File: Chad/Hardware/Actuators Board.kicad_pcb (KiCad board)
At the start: 4 copper layers, 50 x 50 mm, 130 parts, among them IC1 BD62120AEFJ-E2, J1 Conn_01x05_Male, J2 Solenoid(Sol), J3 USB_C_Receptacle_USB2.0, J4 Conn_01x03_Male, J5 Conn_01x06_Male, J6 Conn_01x02_Male, Q1 MMDT2222A, Q2 SI2366DS, U1 ESP32-PICO-D4, U2 TPS54233D, U3 CP2102-GMR-QFN28, U4 SN65HVD230, U5 LTC4411, U6 RT9025-25GSP, U7 LTC4411

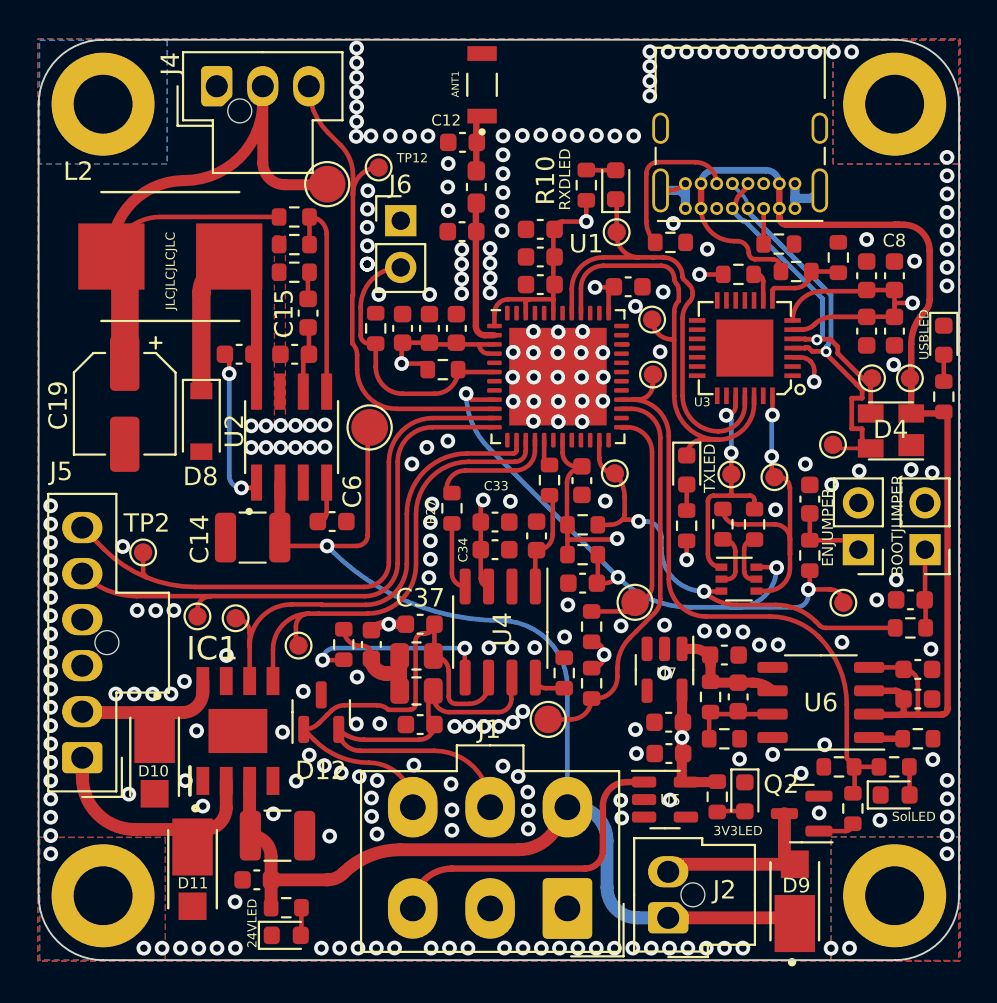
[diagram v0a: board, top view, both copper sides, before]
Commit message: Cut down on the number of vias, changed folder structure
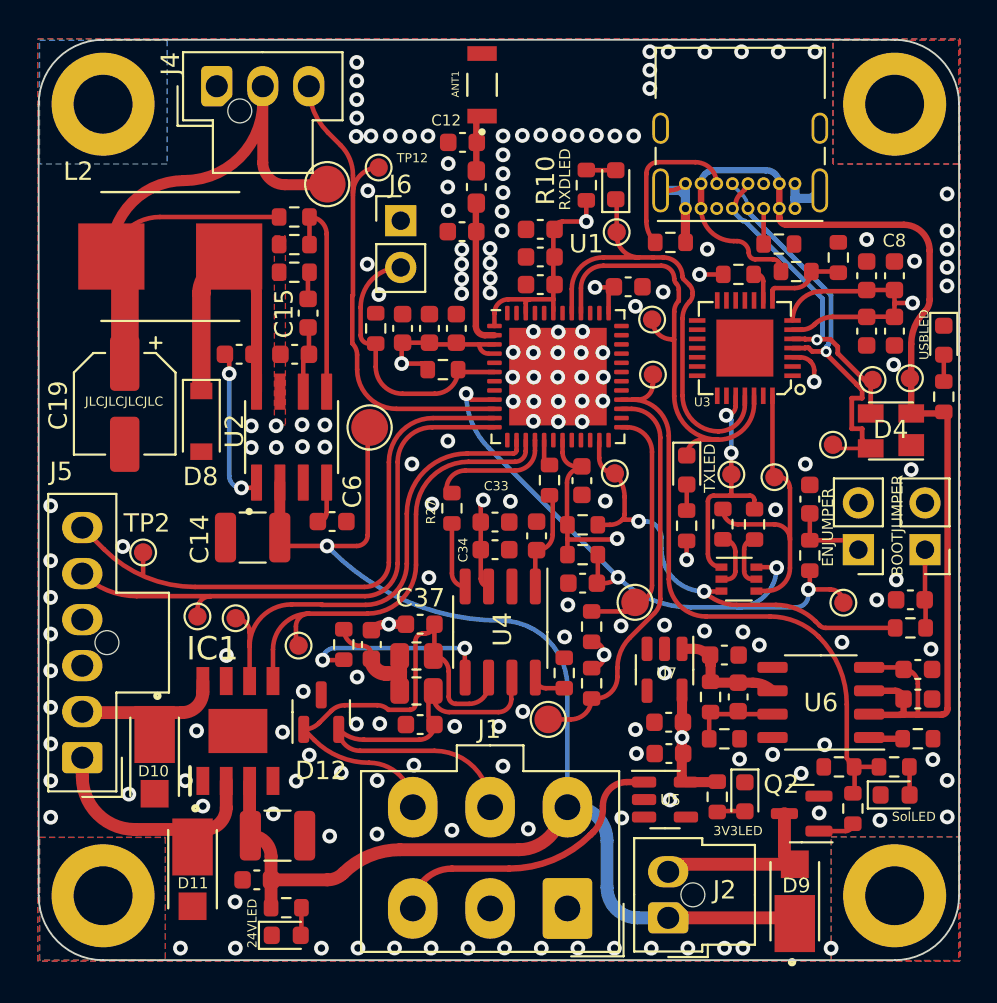
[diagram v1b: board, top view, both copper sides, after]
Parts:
- moved TP17 0.09 mm to (100.3, 48.5)
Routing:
- net /Motor+: track 14.7 -> 11.1 mm
- net +24V: track 79.9 -> 76.9 mm
- net +6V: track 38.6 -> 36.2 mm
- net /Motor-: track 10.1 -> 7.80 mm
- net VBUS: track 64.2 -> 62.2 mm
- net +3V3: track 64.6 -> 62.9 mm
- net /CAN_HIGH: track 25.1 -> 23.6 mm
- net /DTR: track 18.1 -> 16.6 mm, vias 2 -> 0
- net GND: track 11.6 -> 13.1 mm, vias 256 -> 171
- net Net-(J1-Pad3): track 17.4 -> 15.9 mm
- net /CAN_LOW: track 27.8 -> 26.7 mm
- net Net-(C1-Pad1): track 4.39 -> 3.59 mm
- net /USB -> UART/Data+: track 22.9 -> 22.3 mm
- net Net-(C35-Pad1): track 6.77 -> 6.14 mm
- net /SolEN: track 33.6 -> 33.0 mm
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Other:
- board text added: "C.H.A.D-v1"
- board text removed: "C.H.A.D - v1"

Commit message: Implemented design review feedback
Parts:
- removed TP22, TP25: TestPoint, TestPoint:TestPoint_Pad_D1.5mm
- added J7: Endstop Switch 1, TestPoint:TestPoint_Pad_D1.5mm, F.Cu at (87.4, 60.6)
- added J8: Endstop Switch 2, TestPoint:TestPoint_Pad_D1.5mm, F.Cu at (82.7, 66.9)
- 3V3LED1: renamed from 3V3LED; value PWR_LED -> 3V3LED
- C1, C2, C3: value 1uF -> 0.1uF
- C24: value 0.1uF -> 10uF
- L2: value ETQP5M -> 33uH
- moved TP17 0.14 mm to (100.4, 48.4)
- renumbered 24VLED to 24VLED1, BOOTJUMPER to BOOTJUMPER1, ENJUMPER to ENJUMPER1, RXDLED to RXLED1, SolLED to SolLED1, TXLED to TXLED1, USBLED to USBLED1
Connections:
- R19 pad 2: GND -> +3V3
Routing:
- net GND: track 13.1 -> 19.2 mm, vias 171 -> 170
- net +3V3: track 62.9 -> 64.1 mm, vias 10 -> 11
- net /USB -> UART/Data-: track 19.8 -> 20.4 mm
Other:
- board text added: "24VLED"
- board text added: "24V_TP"
- board text added: "3V3LED"
- board text added: "6V_TP"
- board text added: "BOOTJUMPER"
- board text added: "DCMotor_Conn"
- board text added: "DTR_TP"
- board text added: "DirPin1_TP"
- board text added: "DirPin2_TP"
- board text added: "ENJUMPER"
- board text added: "ES1Pad"
- board text added: "ES2Pad"
- board text added: "HallS1_TP"
- board text added: "HallS2_TP"
- board text added: "RBUS"
- board text added: "RTS_TP"
- board text added: "RXLED"
- board text added: "SSR_Conn"
- board text added: "ServoPWM_TP"
- board text added: "Servo_Conn"
- board text added: "SolLED"
- board text added: "Sol_Conn"
- board text added: "TXLED"
- board text added: "USBLED"

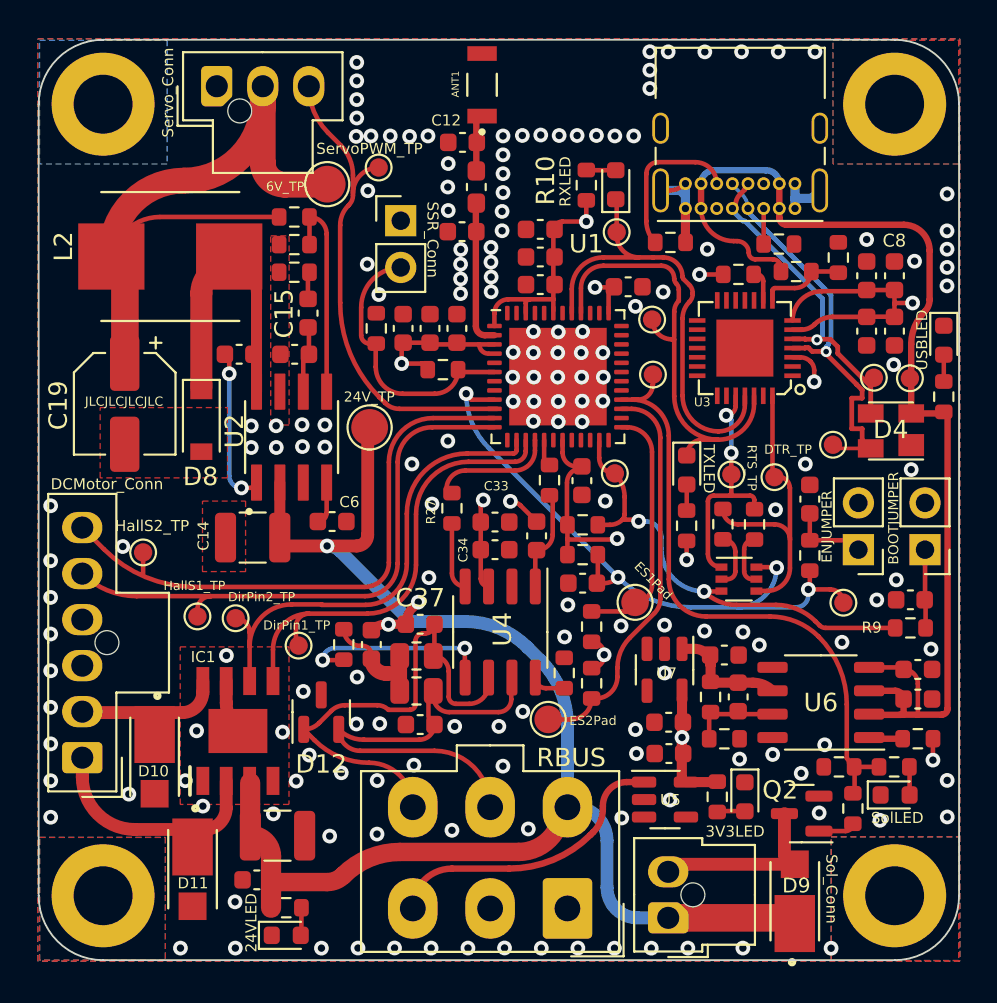
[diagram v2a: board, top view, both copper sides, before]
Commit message: Reduced thermal relief for the higher current connectors
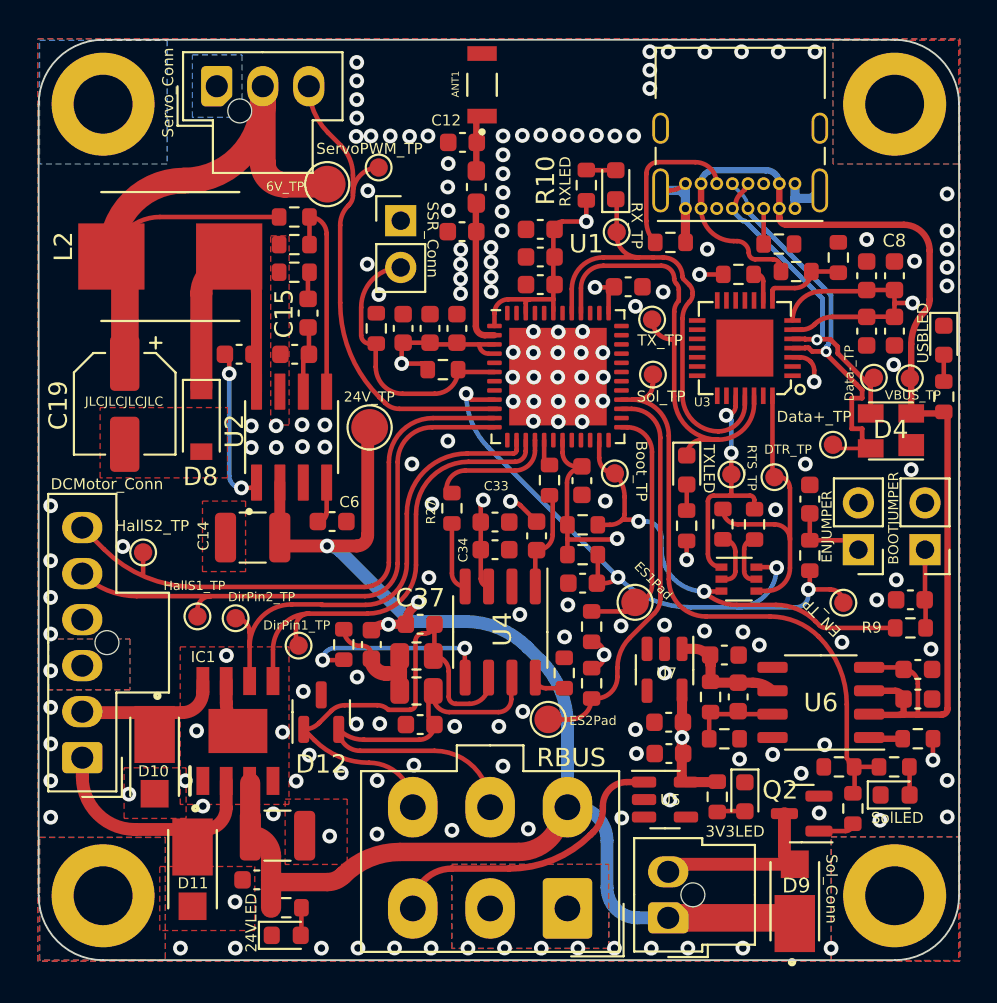
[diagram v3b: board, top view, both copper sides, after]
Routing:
- net GND: vias 170 -> 171
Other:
- board text added: "Boot_TP"
- board text added: "Data+_TP"
- board text added: "Data-_TP"
- board text added: "EN_TP"
- board text added: "RX_TP"
- board text added: "Sol_TP"
- board text added: "TX_TP"
- board text added: "VBUS_TP"
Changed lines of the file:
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@@
     (effects (font (size 1 1) (thickness 0.15)) (justify left mirror))
   )
+  (gr_text "RX_TP" (at 87.49 40.09 270) (layer "F.SilkS")
+    (effects (font (size 0.6 0.6) (thickness 0.1)))
+  )
+  (gr_text "Data+_TP\n" (at 97.12 50.48) (layer "F.SilkS")
+    (effects (font (size 0.6 0.6) (thickness 0.1)))
+  )
   (gr_text "SolLED\n" (at 101.64 72.27) (layer "F.SilkS")
     (effects (font (size 0.6 0.6) (thickness 0.1)))
@@
   (gr_text "24VLED" (at 66.55 77.97 90) (layer "F.SilkS")
     (effects (font (size 0.6 0.6) (thickness 0.1)))
+  )
+  (gr_text "Data-_TP\n" (at 99.04 48.11 90) (layer "F.SilkS")
+    (effects (font (size 0.5 0.5) (thickness 0.1)))
   )
   (gr_text "DCMotor_Conn" (at 58.71 54.14) (layer "F.SilkS")
@@
     (effects (font (size 0.5 0.5) (thickness 0.1)))
   )
+  (gr_text "VBUS_TP" (at 102.49 49.31) (layer "F.SilkS")
+    (effects (font (size 0.5 0.5) (thickness 0.1)))
+  )
   (gr_text "BOOTJUMPER\n" (at 101.44 55.99 90) (layer "F.SilkS")
     (effects (font (size 0.55 0.55) (thickness 0.1)))
@@
     (effects (font (size 0.6 0.6) (thickness 0.1)))
   )
+  (gr_text "Boot_TP" (at 87.74 53.43 270) (layer "F.SilkS")
+    (effects (font (size 0.6 0.6) (thickness 0.1)))
+  )
   (gr_text "TXLED\n" (at 91.41 53.31 270) (layer "F.SilkS")
+    (effects (font (size 0.6 0.6) (thickness 0.1)))
+  )
+  (gr_text "TX_TP" (at 88.76 46.33) (layer "F.SilkS")
     (effects (font (size 0.6 0.6) (thickness 0.1)))
   )
@@
     (effects (font (size 0.6 0.6) (thickness 0.1)))
   )
-  (gr_text "USBLED\n" (at 102.99 46.31 90) (layer "F.SilkS")
+  (gr_text "USBLED\n" (at 103.04 45.93 90) (layer "F.SilkS")
     (effects (font (size 0.6 0.6) (thickness 0.1)))
   )
@@
     (effects (font (size 0.55 0.55) (thickness 0.1)))
   )
+  (gr_text "EN_TP" (at 97.54 61.39 135) (layer "F.SilkS")
+    (effects (font (size 0.6 0.6) (thickness 0.1)))
+  )
   (gr_text "RBUS" (at 83.93 69) (layer "F.SilkS")
     (effects (font (size 1 1) (thickness 0.15)))
@@
   (gr_text "RTS_TP" (at 93.74 53.25 270) (layer "F.SilkS")
     (effects (font (size 0.5 0.5) (thickness 0.1)))
+  )
+  (gr_text "Sol_TP" (at 88.81 49.38) (layer "F.SilkS")
+    (effects (font (size 0.6 0.6) (thickness 0.1)))
   )
   (gr_text "ENJUMPER\n" (at 97.82 56.45 90) (layer "F.SilkS")
@@
   (via (at 81.3 66.49) (size 0.8) (drill 0.4) (layers "F.Cu" "B.Cu") (free) (net 2))
   (via (at 55.654 62.281) (size 0.8) (drill 0.4) (layers "F.Cu" "B.Cu") (free) (net 2))
+  (via (at 81.14 61.22) (size 0.8) (drill 0.4) (layers "F.Cu" "B.Cu") (free) (net 2))
   (via (at 94.875 68.825) (size 0.8) (drill 0.4) (layers "F.Cu" "B.Cu") (free) (net 2))
   (via (at 70.361 79.346) (size 0.8) (drill 0.4) (layers "F.Cu" "B.Cu") (free) (net 2))
@@
   (segment (start 102.3125 69.530177) (end 102.3125 71.025) (width 0.25) (layer "F.Cu") (net 108))
   (segment (start 104.17 48.565) (end 104.17 47.11) (width 0.25) (layer "F.Cu") (net 109))
+  (zone (net 2) (net_name "GND") (layer "F.Cu") (name "Hbridgethermalreliefreduction") (hatch edge 0.508)
+    (priority 10)
+    (connect_pads (clearance 0.254))
+    (min_thickness 0.254) (filled_areas_thickness no)
+    (fill yes (thermal_gap 0.254) (thermal_bridge_width 1))
+    (polygon
+      (pts
+        (xy 66.74 78.39)
+        (xy 61.58 78.39)
+        (xy 61.58 74.91)
+        (xy 66.74 74.91)
+      )
+    )
+  )
   (zone (net 0) (net_name "") (layer "F.Cu") (hatch edge 0.508)
     (connect_pads (clearance 0))
@@
     )
   )
+  (zone (net 2) (net_name "GND") (layers "F.Cu" "In1.Cu" "B.Cu") (name "Hbridgethermalreliefreduction") (hatch edge 0.508)
+    (priority 10)
+    (connect_pads (clearance 0.254))
+    (min_thickness 0.254) (filled_areas_thickness no)
+    (fill yes (thermal_gap 0.254) (thermal_bridge_width 1))
+    (polygon
+      (pts
+        (xy 59.96 65.31)
+        (xy 55.53 65.31)
+        (xy 55.53 62.55)
+        (xy 59.96 62.55)
+      )
+    )
+  )
   (zone (net 0) (net_name "") (layer "F.Cu") (hatch edge 0.508)
     (connect_pads (clearance 0))
@@
     )
   )
+  (zone (net 2) (net_name "GND") (layer "F.Cu") (name "Hbridgethermalreliefreduction") (hatch edge 0.508)
+    (priority 10)
+    (connect_pads (clearance 0.2))
+    (min_thickness 0.254) (filled_areas_thickness no)
+    (fill yes (thermal_gap 0.254) (thermal_bridge_width 1))
+    (polygon
+      (pts
+        (xy 71.76 74.8)
+        (xy 68.39 74.8)
+        (xy 68.39 71.25)
+        (xy 71.76 71.25)
+      )
+    )
+  )
   (zone (net 2) (net_name "GND") (layers "F.Cu" "In1.Cu" "B.Cu") (name "No thermal relief plane") (hatch edge 0.508)
     (priority 2)
@@
         (xy 98.05 73.3)
         (xy 104.98 73.3)
+      )
+    )
+  )
+  (zone (net 2) (net_name "GND") (layers "F.Cu" "In1.Cu" "B.Cu") (name "Hbridgethermalreliefreduction") (hatch edge 0.508)
+    (priority 10)
+    (connect_pads (clearance 0.2))
+    (min_thickness 0.254) (filled_areas_thickness no)
+    (fill yes (thermal_gap 0.254) (thermal_bridge_width 1))
+    (polygon
+      (pts
+        (xy 85.97 79.36)
+        (xy 77.44 79.36)
+        (xy 77.44 74.79)
+        (xy 85.97 74.79)
       )
     )
@@
     )
   )
+  (zone (net 2) (net_name "GND") (layer "F.Cu") (name "Hbridgethermalreliefreduction") (hatch edge 0.508)
+    (priority 10)
+    (connect_pads (clearance 0.254))
+    (min_thickness 0.254) (filled_areas_thickness no)
+    (fill yes (thermal_gap 0.254) (thermal_bridge_width 1))
+    (polygon
+      (pts
+        (xy 63.01 72.3)
+        (xy 59.64 72.3)
+        (xy 59.64 69.55)
+        (xy 63.01 69.55)
+      )
+    )
+  )
+  (zone (net 4) (net_name "+3V3") (layer "In2.Cu") (name "Hbridgethermalreliefreduction") (hatch edge 0.508)
+    (priority 10)
+    (connect_pads (clearance 0.2))
+    (min_thickness 0.254) (filled_areas_thickness no)
+    (fill yes (thermal_gap 0.254) (thermal_bridge_width 1))
+    (polygon
+      (pts
+        (xy 59.88 62.57)
+        (xy 55.9 62.57)
+        (xy 55.9 60.09)
+        (xy 59.88 60.09)
+      )
+    )
+  )
   (zone (net 4) (net_name "+3V3") (layer "In2.Cu") (hatch edge 0.508)
     (connect_pads (clearance 0.508))
@@
       )
     )
+  )
+  (zone (net 2) (net_name "GND") (layers "In1.Cu" "B.Cu") (name "Hbridgethermalreliefreduction") (hatch edge 0.508)
+    (priority 10)
+    (connect_pads (clearance 0.254))
+    (min_thickness 0.254) (filled_areas_thickness no)
+    (fill yes (thermal_gap 0.254) (thermal_bridge_width 1))
+    (polygon
+      (pts
+        (xy 66.05 34.21)
+        (xy 63.35 34.21)
+        (xy 63.35 30.82)
+        (xy 66.05 30.82)
+      )
+    )

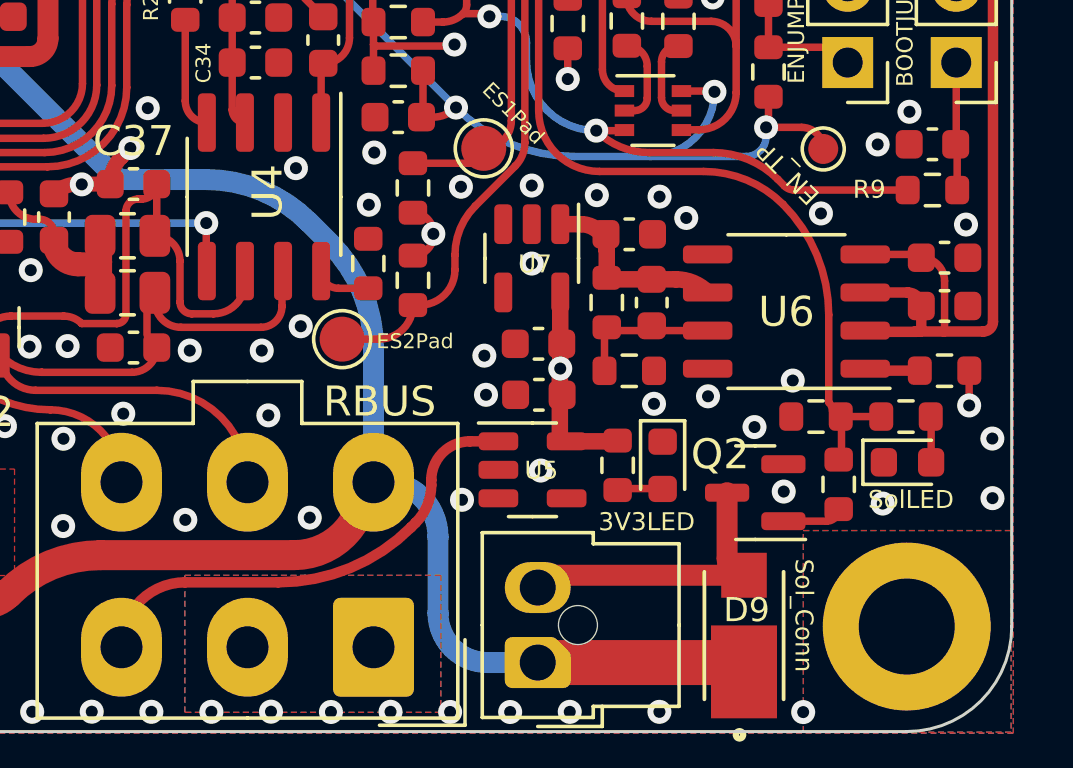
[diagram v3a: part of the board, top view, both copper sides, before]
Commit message: Changed LDO footprint to include exposed pad
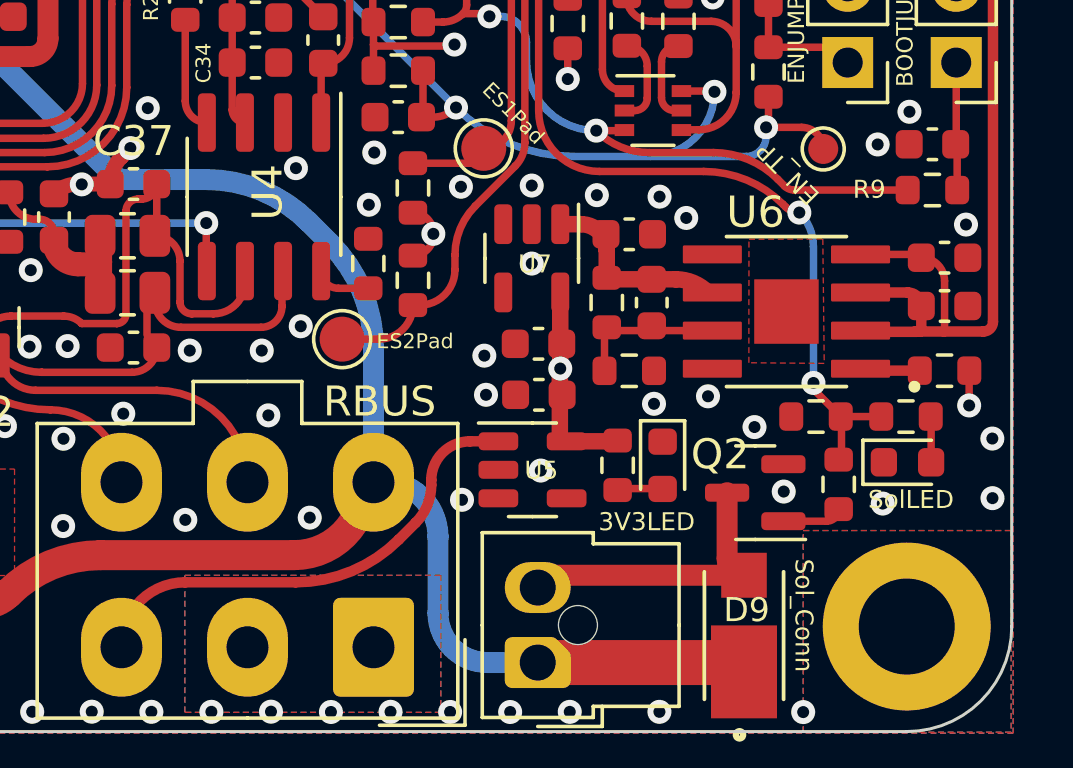
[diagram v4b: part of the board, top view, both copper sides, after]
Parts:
- C11: value 1.2pF -> 33pF
- C12: value 1.5pF -> 100pF
- U6: footprint Package_SO:SOP-8_3.9x4.9mm_P1.27mm -> iclr:SOIC127P599X175-9N
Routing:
- net /SolEN: track 33.0 -> 33.6 mm, vias 0 -> 2
- net GND: vias 171 -> 169

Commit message: change resistor values for new LDO
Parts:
- removed C21: 1uF, Capacitor_SMD:C_0603_1608Metric
- removed C24: 10uF, Capacitor_SMD:C_0603_1608Metric
- removed the G*** at (62.0, 41.3)
- removed R19: 100k, Resistor_SMD:R_0603_1608Metric
- R24: value 147k -> 56k
- R25: value 47k -> 10k
- moved C20 1.37 mm to (101.9, 64.7), turned to -90 degrees
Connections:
- R24 pad 2: Net-(C24-Pad1) -> (no net)
- R25 pad 1: Net-(C24-Pad1) -> Net-(R24-Pad2)
- U6 pad 1: Net-(R19-Pad1) -> unconnected-(U6-Pad1)
- U6 pad 4: VBUS -> unconnected-(U6-Pad4)
- U6 pad 7: Net-(C24-Pad1) -> Net-(R24-Pad2)
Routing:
- net VBUS: track 62.2 -> 54.7 mm
- net Net-(R24-Pad2): track 0.00 -> 4.63 mm
- net Net-(C24-Pad1): track 4.63 -> 0.00 mm
- net Net-(R19-Pad1): track 1.75 -> 0.00 mm
- net +3V3: track 64.1 -> 62.9 mm, vias 11 -> 10
